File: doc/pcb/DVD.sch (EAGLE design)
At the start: 37 parts, among them IC2 74HC14N, IC3 7805

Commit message: PCB updates
Moved voltage regulator
Checked that the OKI switching regulator would also fit (it does)
Moved capacitors around voltage regulator
Moved motor pins but couldn't make one square
Made other pin 1 square
Added more vias to the ground copper pour
Re-loaded DRC from PCB house and made necessary changes
Increased isolation of copper pour as much as possible (0.005->0.012)
in order to sleep better :-)
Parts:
- LED1, LED2: device adafruit:LED5MM -> adafruit:LED3MM
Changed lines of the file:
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@@
 <layer number="17" name="Pads" color="2" fill="1" visible="yes" active="no"/>
 <layer number="18" name="Vias" color="2" fill="1" visible="yes" active="no"/>
-<layer number="19" name="Unrouted" color="6" fill="1" visible="yes" active="no"/>
+<layer number="19" name="Unrouted" color="11" fill="1" visible="yes" active="no"/>
 <layer number="20" name="Dimension" color="15" fill="1" visible="yes" active="no"/>
 <layer number="21" name="tPlace" color="7" fill="1" visible="yes" active="no"/>
@@
 <part name="U$3" library="DVD" deviceset="BNO055_LIGHT" device=""/>
 <part name="R8" library="resistor" deviceset="R-EU_" device="0207/10" value="220"/>
-<part name="LED1" library="adafruit" deviceset="LED" device="5MM" value="Amber"/>
+<part name="LED1" library="adafruit" deviceset="LED" device="3MM" value="Amber"/>
 <part name="R9" library="resistor" deviceset="R-EU_" device="0207/10" value="220"/>
-<part name="LED2" library="adafruit" deviceset="LED" device="5MM" value="Green"/>
+<part name="LED2" library="adafruit" deviceset="LED" device="3MM" value="Green"/>
 <part name="C5" library="rcl" deviceset="C-EU" device="025-024X044" value="100nF"/>
 <part name="JP14" library="pinhead" deviceset="PINHD-1X1" device="" value="P17"/>

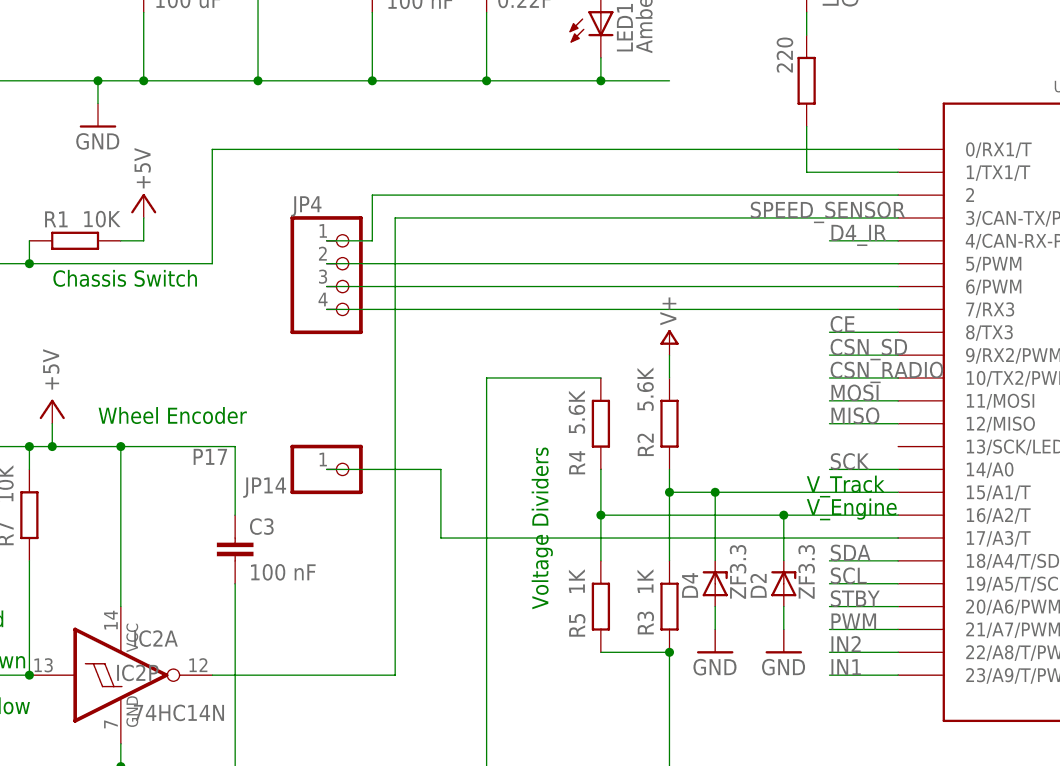
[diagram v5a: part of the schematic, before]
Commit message: PCB and Schematic Updates
- Added 2-pin jumper for +5V and GND near the 4-pin header with
  spare signal pins
- Added Langloecher
- Cut the lower corners of the PCB to make it fit into the car
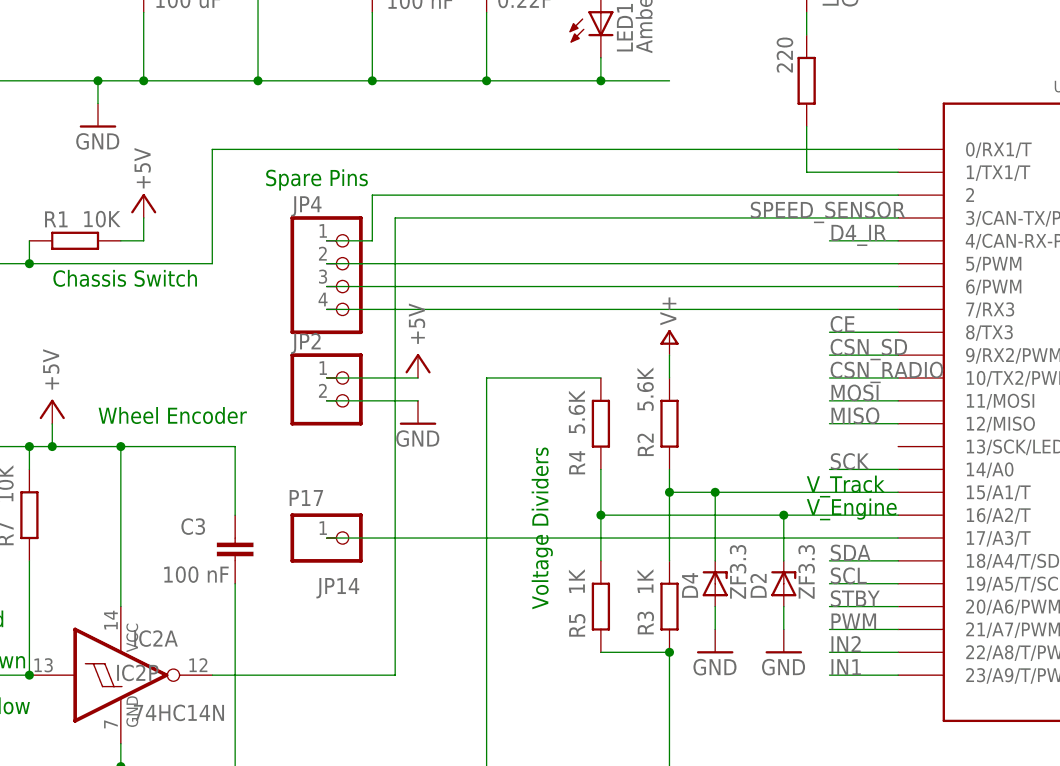
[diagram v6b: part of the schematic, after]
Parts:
- added JP2: (no value), pinhead:PINHD-1X2
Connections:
- net +5V: now also JP2.1
- net GND: now also JP2.2
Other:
- note added: "Spare Pins"
- moved on the sheet: JP14
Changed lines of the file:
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@@
 <part name="JP1" library="pinhead" deviceset="PINHD-1X2" device="" value="Pick-up"/>
 <part name="IC3" library="linear" deviceset="78*" device="TV" technology="6" value="7805"/>
+<part name="JP2" library="pinhead" deviceset="PINHD-1X2" device=""/>
+<part name="P+12" library="supply1" deviceset="+5V" device=""/>
+<part name="GND16" library="supply1" deviceset="GND" device=""/>
 </parts>
 <sheets>
@@
 <text x="3.048" y="69.342" size="1.778" layer="91">brown</text>
 <text x="3.302" y="64.262" size="1.778" layer="91">yellow</text>
+<text x="36.322" y="122.936" size="1.778" layer="91">Spare Pins</text>
 </plain>
 <instances>
@@
 </instance>
 <instance part="C2" gate="G$1" x="60.96" y="147.32"/>
-<instance part="C3" gate="G$1" x="33.02" y="83.82"/>
+<instance part="C3" gate="G$1" x="33.02" y="83.82" smashed="yes">
+<attribute name="NAME" x="26.924" y="84.201" size="1.778" layer="95"/>
+<attribute name="VALUE" x="24.892" y="78.867" size="1.778" layer="96"/>
+</instance>
 <instance part="C4" gate="G$1" x="195.58" y="76.2" smashed="yes" rot="R90">
 <attribute name="NAME" x="194.056" y="73.279" size="1.778" layer="95" rot="R180"/>
@@
 <instance part="LED2" gate="G$1" x="96.52" y="147.32"/>
 <instance part="C5" gate="G$1" x="205.74" y="45.72"/>
-<instance part="JP14" gate="G$1" x="45.72" y="91.44" smashed="yes">
-<attribute name="NAME" x="34.036" y="88.773" size="1.778" layer="95"/>
-<attribute name="VALUE" x="28.194" y="91.948" size="1.778" layer="96"/>
+<instance part="JP14" gate="G$1" x="45.72" y="83.82" smashed="yes">
+<attribute name="NAME" x="42.164" y="77.597" size="1.778" layer="95"/>
+<attribute name="VALUE" x="38.862" y="87.376" size="1.778" layer="96"/>
 </instance>
 <instance part="P+7" gate="1" x="180.34" y="129.54" smashed="yes">
@@
 </instance>
 <instance part="IC3" gate="A1" x="35.56" y="154.94"/>
+<instance part="JP2" gate="G$1" x="45.72" y="99.06"/>
+<instance part="P+12" gate="1" x="53.34" y="104.14" smashed="yes">
+<attribute name="VALUE" x="54.102" y="105.156" size="1.778" layer="96" rot="R90"/>
+</instance>
+<instance part="GND16" gate="1" x="53.34" y="96.52"/>
 </instances>
 <busses>
@@
 <wire x1="160.02" y1="33.02" x2="160.02" y2="30.48" width="0.1524" layer="91"/>
 </segment>
+<segment>
+<pinref part="GND16" gate="1" pin="GND"/>
+<pinref part="JP2" gate="G$1" pin="2"/>
+<wire x1="53.34" y1="99.06" x2="43.18" y2="99.06" width="0.1524" layer="91"/>
+</segment>
 </net>
 <net name="+5V" class="0">
@@
 <junction x="12.7" y="93.98"/>
 </segment>
+<segment>
+<pinref part="P+12" gate="1" pin="+5V"/>
+<pinref part="JP2" gate="G$1" pin="1"/>
+<wire x1="53.34" y1="101.6" x2="43.18" y2="101.6" width="0.1524" layer="91"/>
+</segment>
 </net>
 <net name="D4_IR" class="0">
@@
 <net name="N$6" class="0">
 <segment>
-<wire x1="106.68" y1="83.82" x2="55.88" y2="83.82" width="0.1524" layer="91"/>
-<wire x1="55.88" y1="83.82" x2="55.88" y2="91.44" width="0.1524" layer="91"/>
+<wire x1="106.68" y1="83.82" x2="43.18" y2="83.82" width="0.1524" layer="91"/>
 <pinref part="JP14" gate="G$1" pin="1"/>
-<wire x1="55.88" y1="91.44" x2="43.18" y2="91.44" width="0.1524" layer="91"/>
 <pinref part="U$4" gate="G$1" pin="17/A3/T"/>
 </segment>

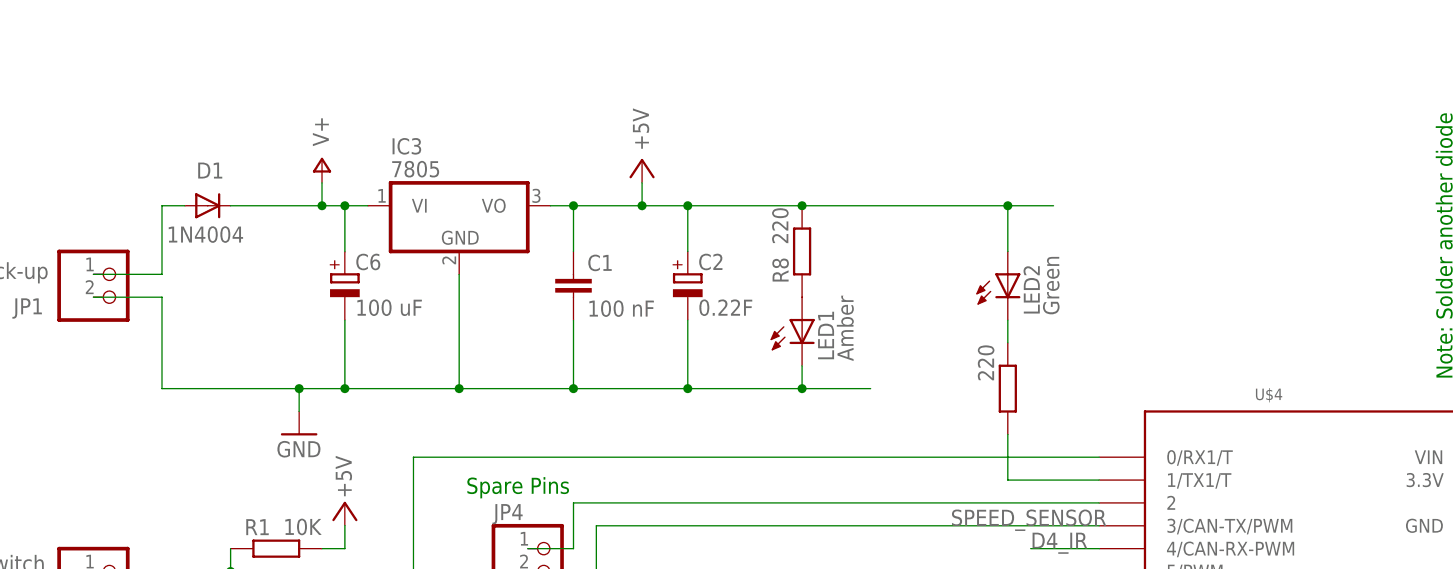
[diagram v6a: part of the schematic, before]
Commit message: Silkscreen cleanup, reconnected Vin to 7805
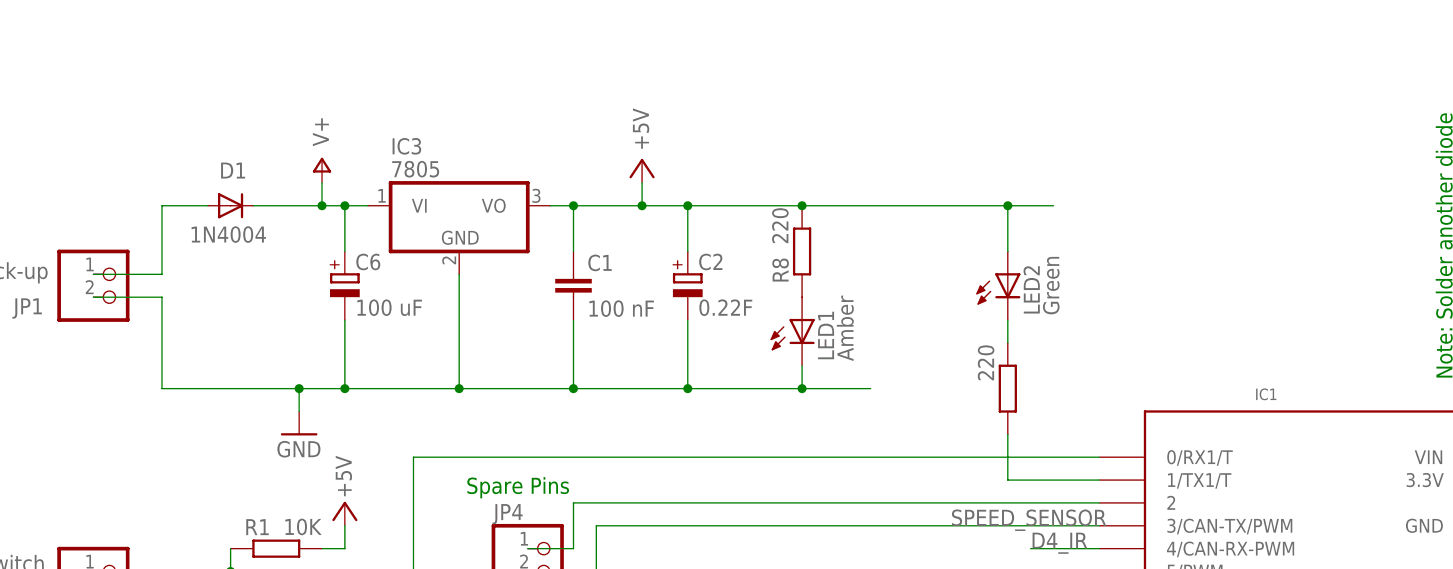
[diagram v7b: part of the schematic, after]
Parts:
- renumbered U$2 to IC4, U$3 to BNO055, U$4 to IC1
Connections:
- net GND: now also IC3.GND
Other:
- moved on the sheet: D1
